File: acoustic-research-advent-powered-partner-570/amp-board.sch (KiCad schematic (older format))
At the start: 126 parts, among them Q1 C546B, Q10 C546B, Q11 C546B, Q12 C556B, Q13 BC33740, Q14 C556B, Q15 KSE3055T, Q16 KSE3055T, Q17 KSE3055T, Q18 BC33740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

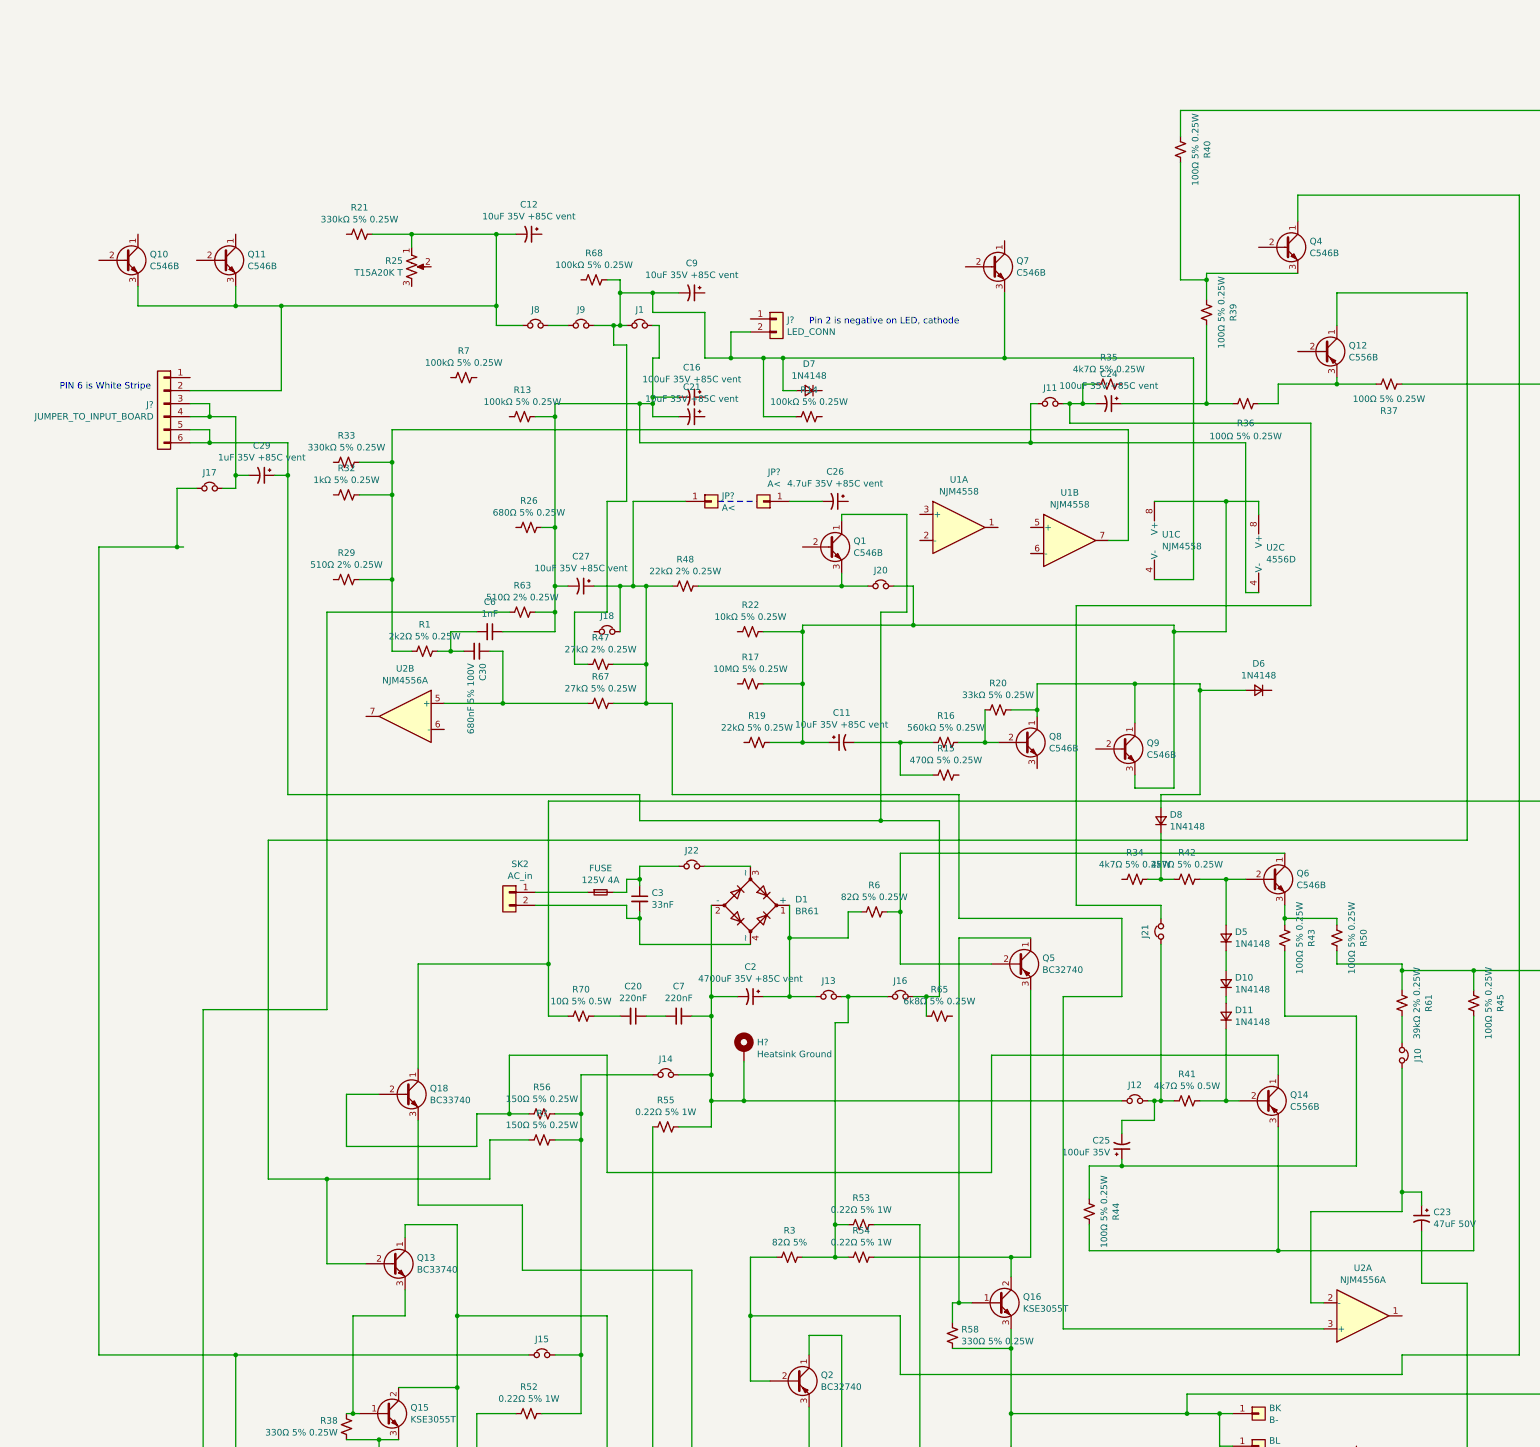
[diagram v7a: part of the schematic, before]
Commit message: finished all potentiometers
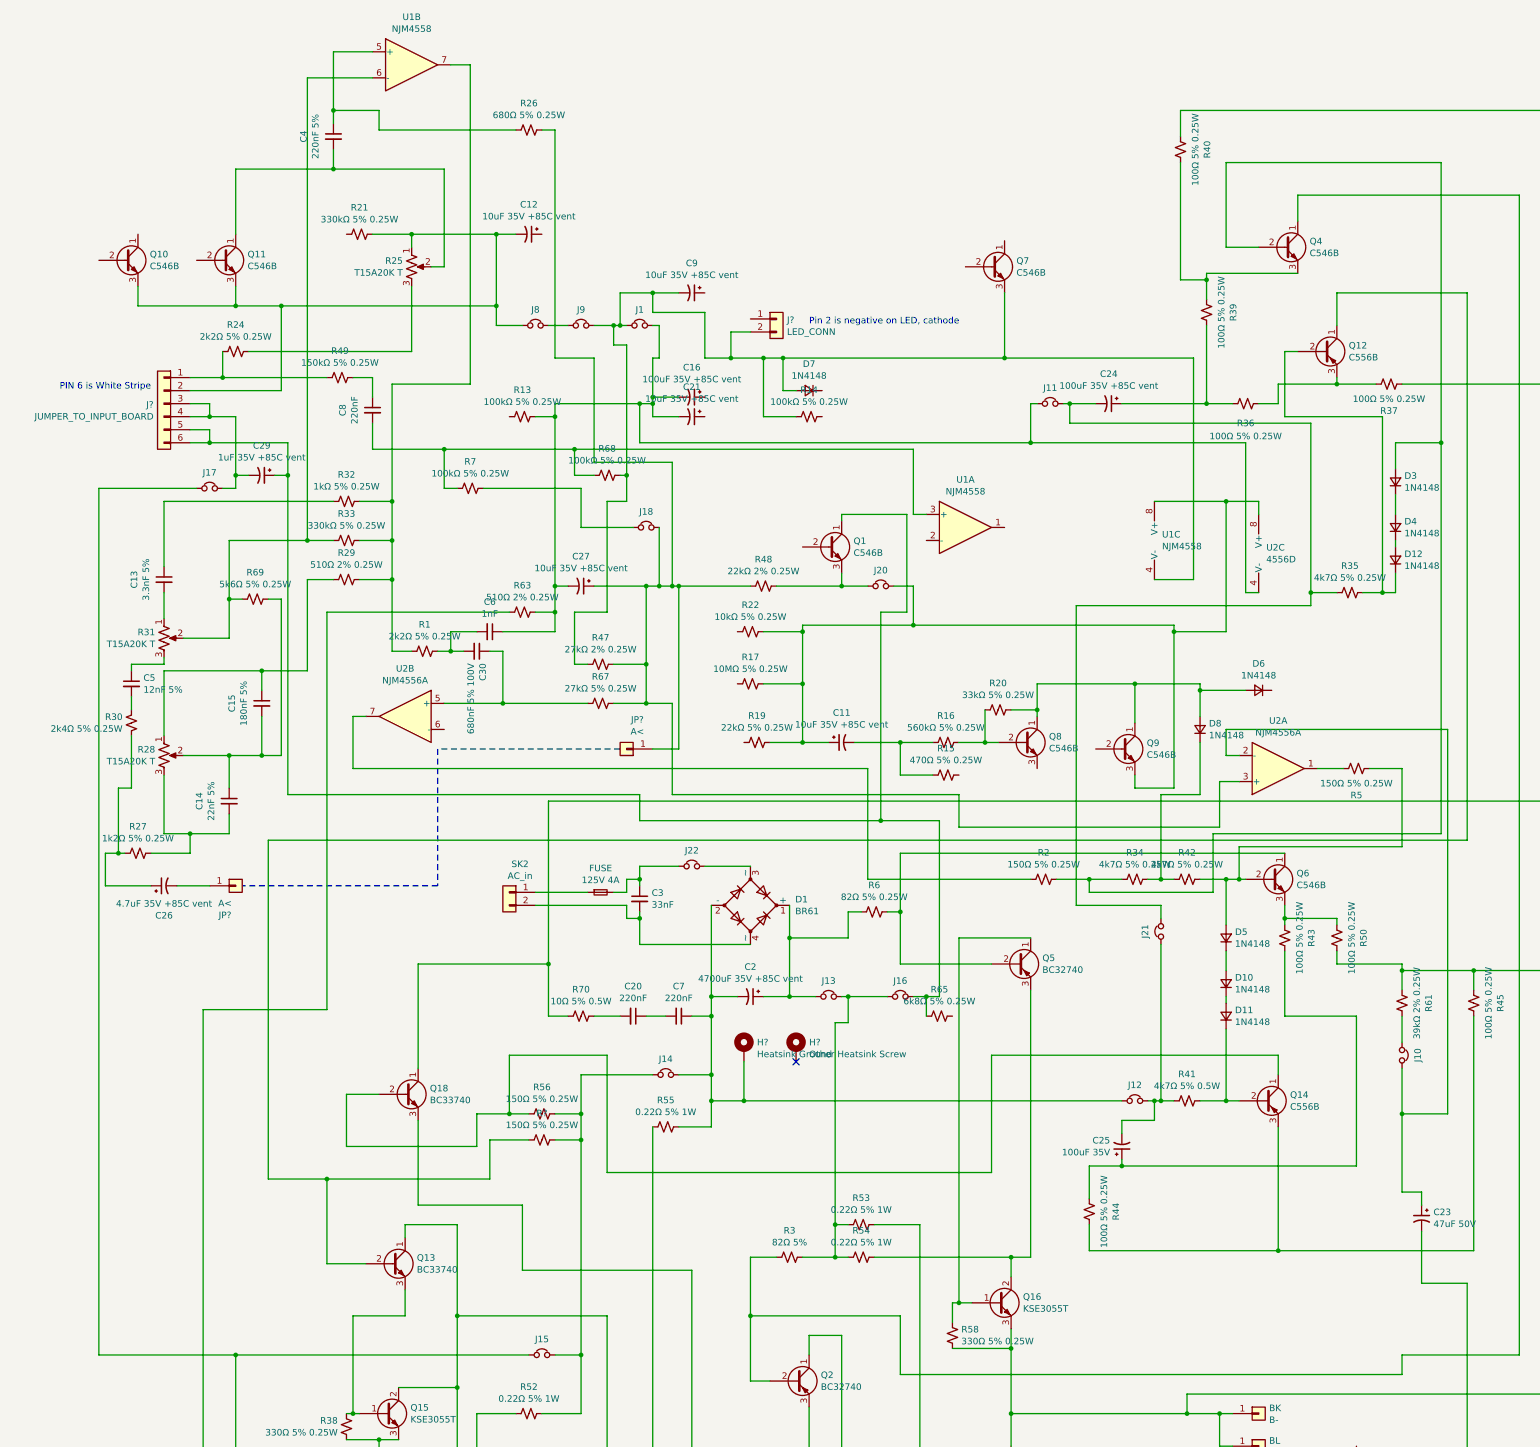
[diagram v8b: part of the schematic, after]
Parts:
- added C13: 3.3nF 5%, symbol Device:C_Small
- added C14: 22nF 5%, symbol Device:C_Small
- added C15: 180nF 5%, symbol Device:C_Small
- added C4: 220nF 5%, symbol Device:C_Small
- added C5: 12nF 5%, symbol Device:C_Small
- added C8: 220nF, symbol Device:C_Small
- added D12, D3, D4: 1N4148, symbol Device:D_Small
- added H?: Other Heatsink Screw, symbol Mechanical:MountingHole_Pad
- added R2, R5: 150Ω 5% 0.25W, symbol Device:R_Small_US
- added R24: 2k2Ω 5% 0.25W, symbol Device:R_Small_US
- added R27: 1k2Ω 5% 0.25W, symbol Device:R_Small_US
- added R28, R31: T15A20K T, symbol Device:R_POT_US
- added R30: 2k4Ω 5% 0.25W, symbol Device:R_Small_US
- added R49: 150kΩ 5% 0.25W, symbol Device:R_Small_US
- added R69: 5k6Ω 5% 0.25W, symbol Device:R_Small_US
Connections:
- net at D5.2 (A), Q6.2 (B), R42.1: now also R5.2
- net at Q12.2 (B): now also R35.1, D12.1 (K)
- net at Q11.1 (C): now also R25.2, C4.2
- net at U2.1: now also R5.1
- net at C27.1, J18.2, JP?.1 (Pin_1)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: now also R26.1
- net at U2.7: now also R2.2
- net at C16.2, C21.2, C27.2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: no longer R26.1
- net at R34.2: now also Q4.2 (B), D3.2 (A), R2.1
- net at U1.3 (+): now also R68.2, R7.2, C8.2
- net at U1.5 (+): now also R26.2, C4.1
- net at U1.6 (-): now also R33.2, R31.2, R69.2
- net at C26.1: now also R27.2, R30.1
- net at J18.1: now also R7.1
- net at R29.2: now also C15.1, R28.1
- net at R32.2: now also C13.1
- net at R25.3: now also R24.1
- net at J?.1 (Pin_1): now also R24.2, R49.2
- new net: C8.1, R49.1
- new net: D3.1 (K), D4.2 (A)
- new net: D12.2 (A), D4.1 (K)
- new net: C13.2, R31.1
- new net: C5.1, R31.3
- new net: C14.1, C15.2, R28.2, R69.1
- new net: C14.2, R27.1, R28.3
- new net: C5.2, R30.2
- no-connect marks 0 -> 1
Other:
- moved on the sheet: C26, D8, J18, JP?, R26, R32, R33, R35, R48, R68, R7, U1A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
